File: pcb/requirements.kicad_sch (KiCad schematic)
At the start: 14 parts

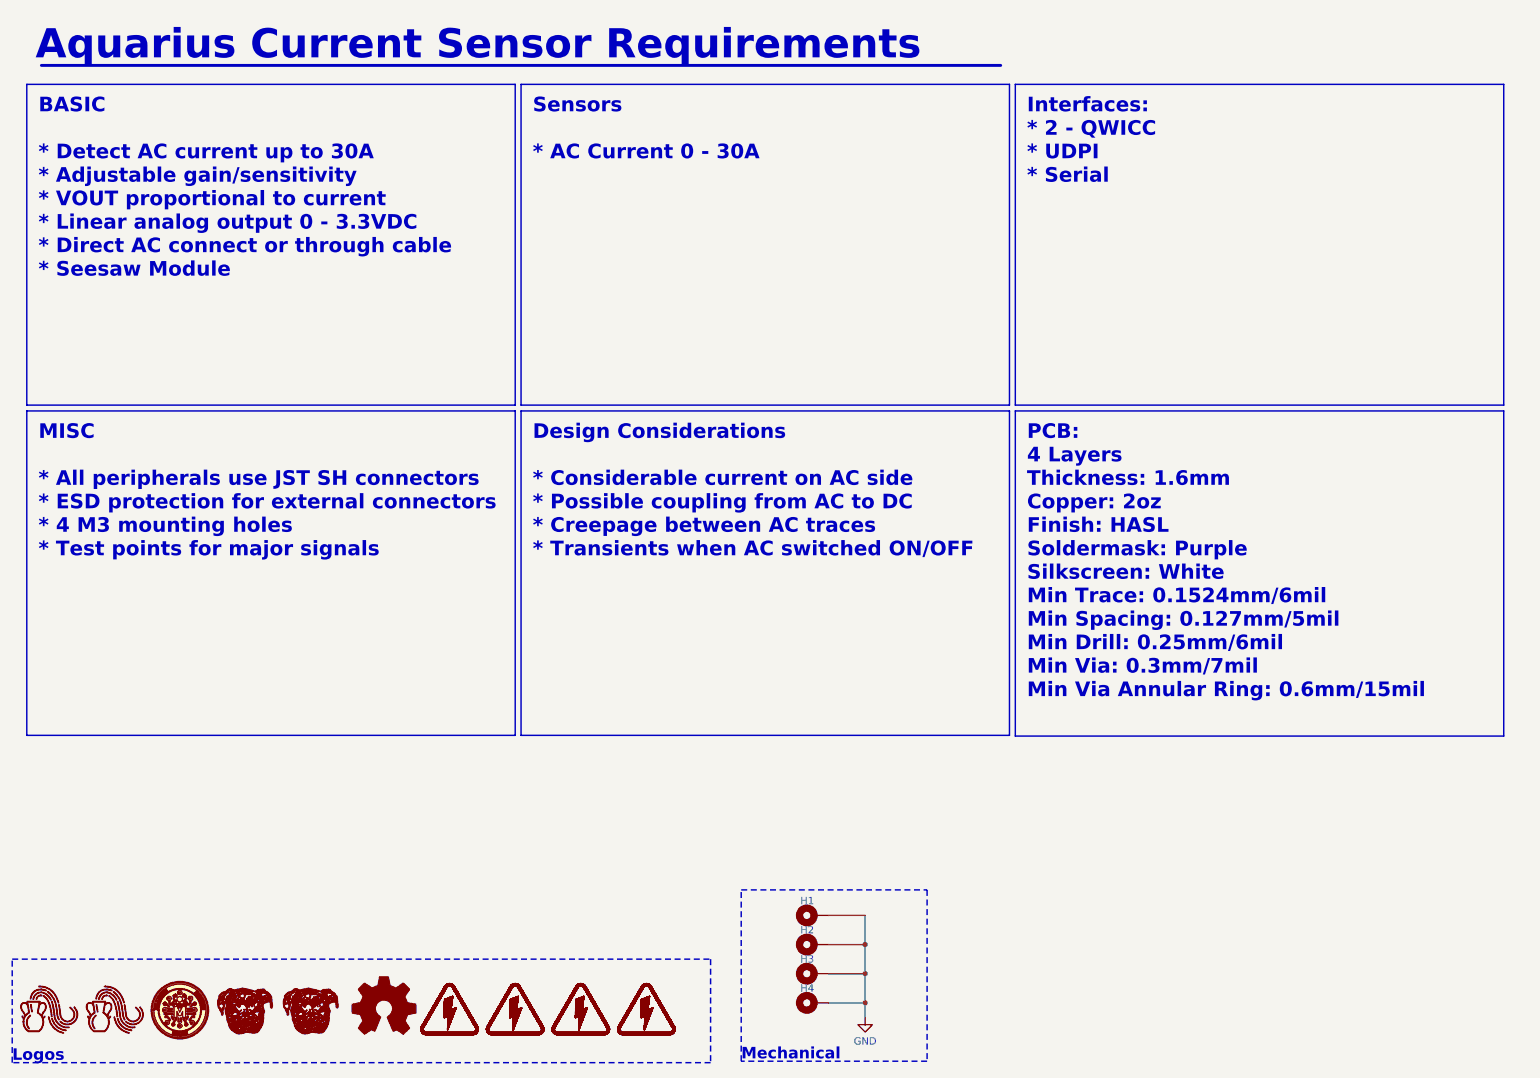
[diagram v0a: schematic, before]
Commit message: refactored to STM32
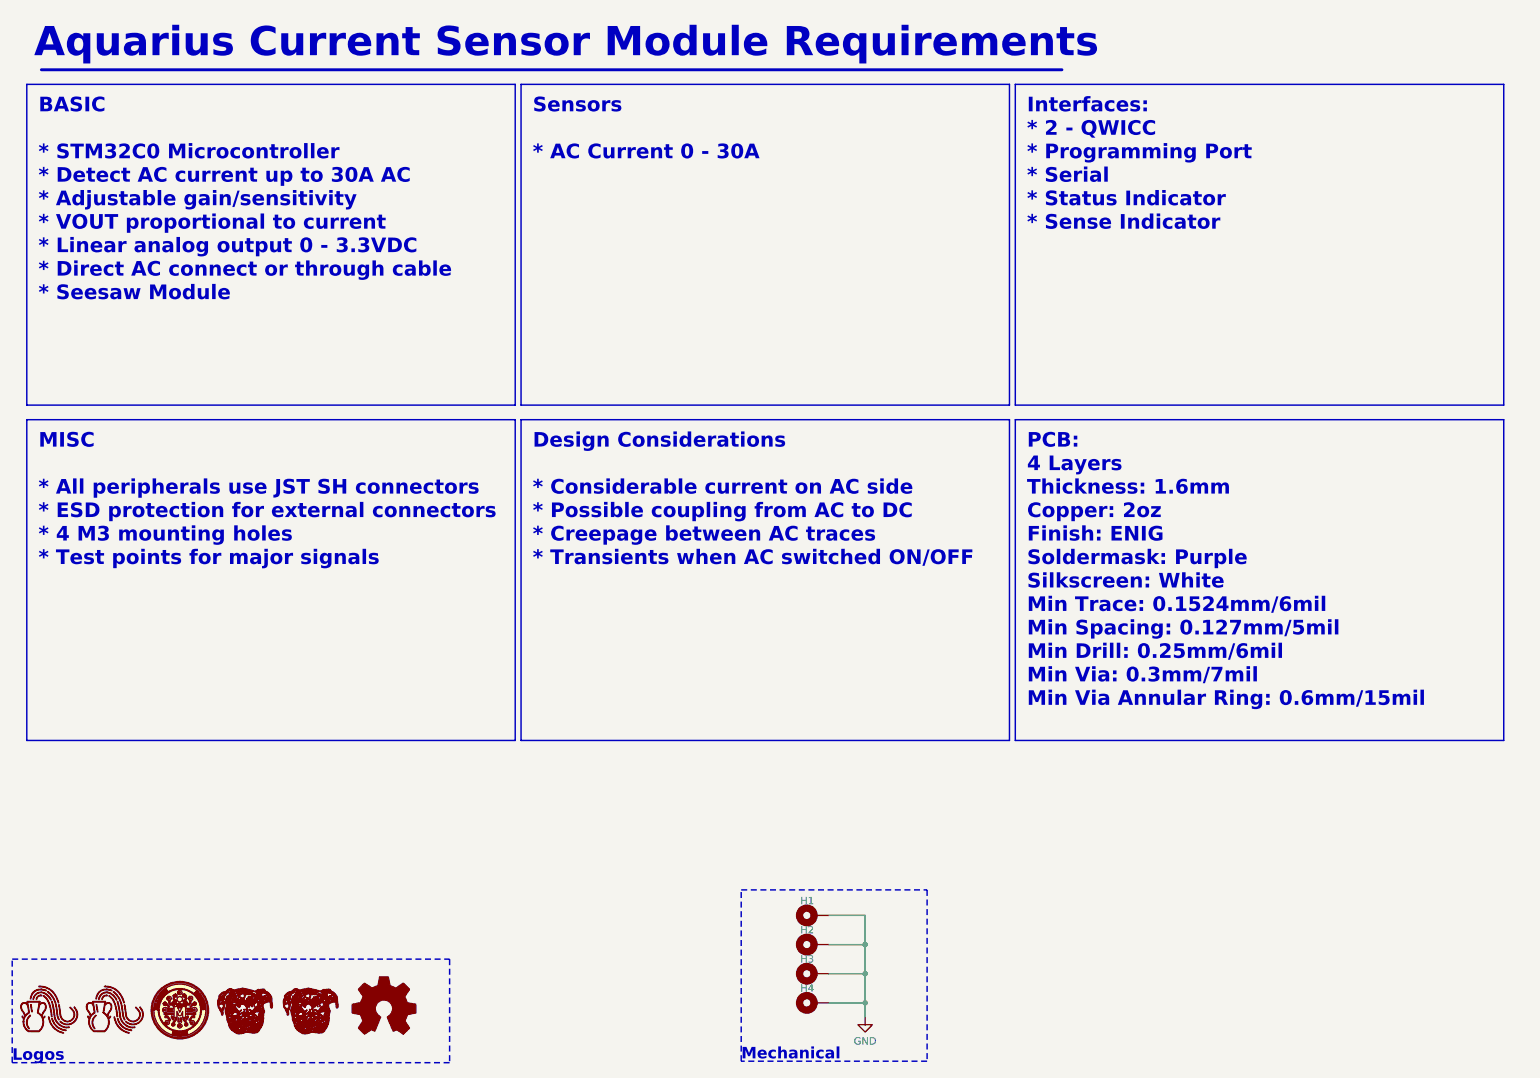
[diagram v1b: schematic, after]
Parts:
- removed SYM1, SYM2, SYM3, SYM4: ~, CRGM Symbols:HIGH-VOLTAGE-5MM, symbol CRGM Symbols:High Voltage
- H1, H2, H3, H4, LOGO1, LOGO3, LOGO4, LOGO5: value ~ -> (none)
- LOGO2: value ~ -> (none); footprint CRGM Logos:Roxy 4mm -> CRGM Logos:Roxy 6.5mm
- LOGO7: value ~ -> (none); footprint CRGM Logos:Aquarius Logo 3.5mm -> CRGM Logos:Aquarius Logo 5mm
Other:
- note added: "Aquarius Current Sensor Module Requirements"
- note removed: "Aquarius Current Sensor Requirements"

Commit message: Added additional silkscreen to AC side
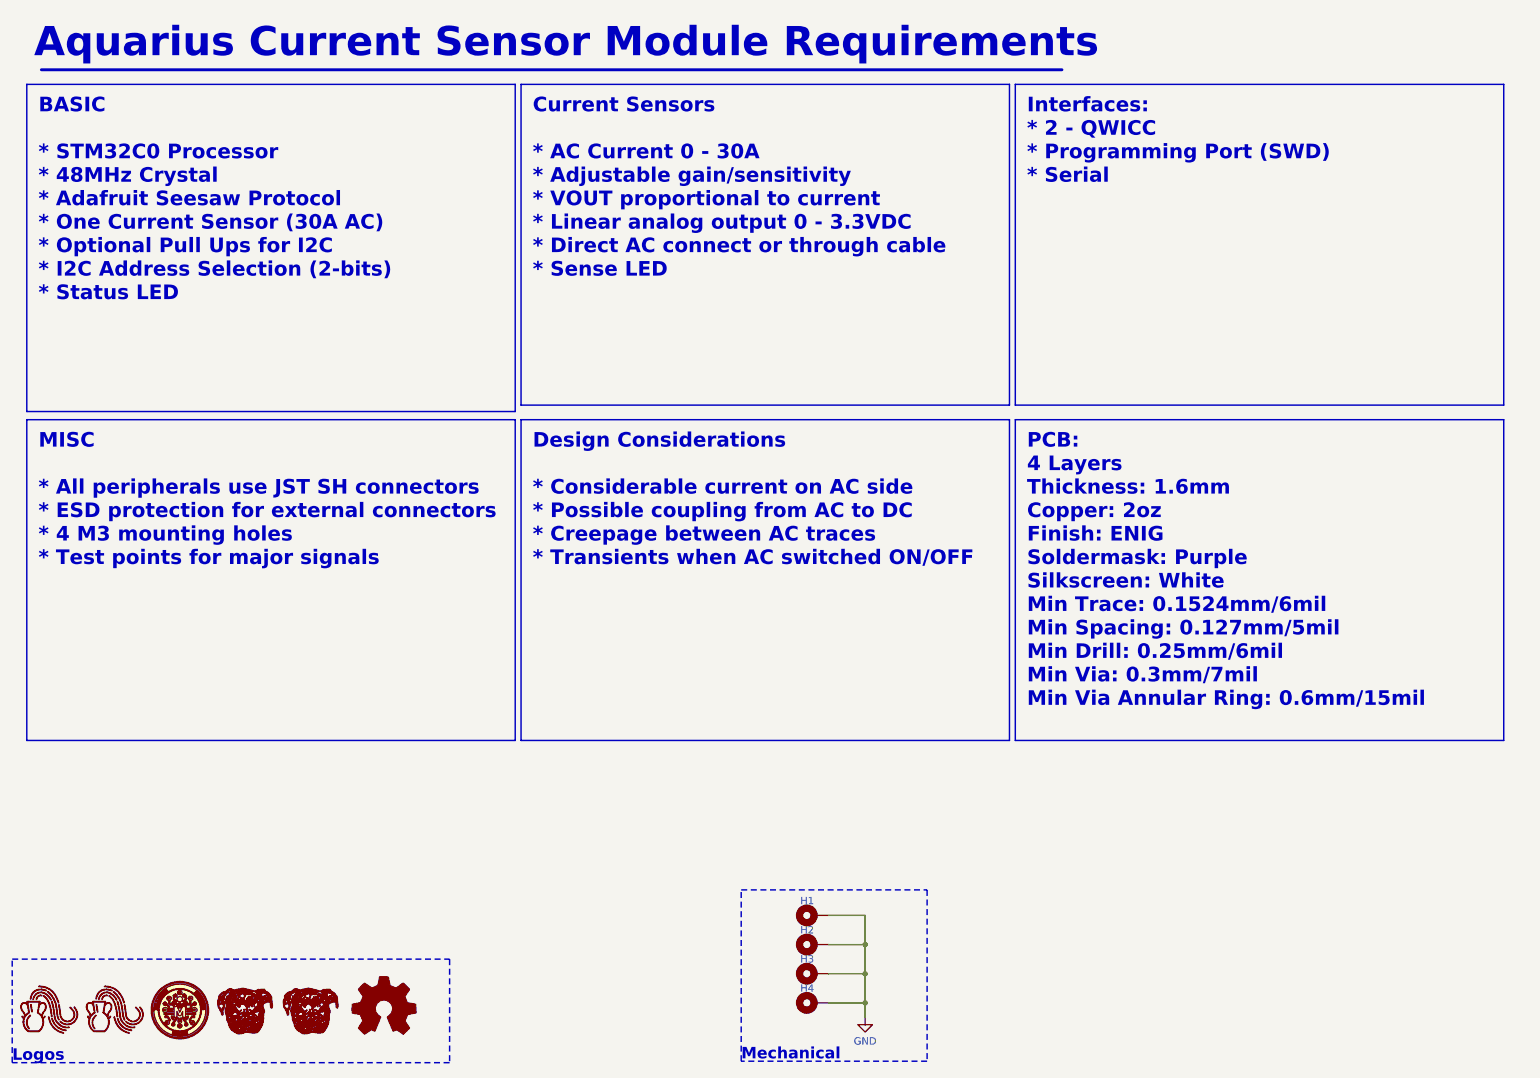
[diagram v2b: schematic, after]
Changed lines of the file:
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@@
 		)
 	)
-	(text_box "Interfaces:\n* 2 - QWICC\n* Programming Port\n* Serial\n* Status Indicator\n* Sense Indicator"
+	(text_box "Interfaces:\n* 2 - QWICC\n* Programming Port (SWD)\n* Serial\n"
 		(exclude_from_sim yes)
 		(at 189.992 25.4 0)
@@
 		)
 	)
-	(text_box "BASIC\n\n* STM32C0 Microcontroller\n* Detect AC current up to 30A AC\n* Adjustable gain/sensitivity\n* VOUT proportional to current\n* Linear analog output 0 - 3.3VDC\n* Direct AC connect or through cable\n* Seesaw Module"
+	(text_box "BASIC\n\n* STM32C0 Processor\n* 48MHz Crystal\n* Adafruit Seesaw Protocol\n* One Current Sensor (30A AC)\n* Optional Pull Ups for I2C\n* I2C Address Selection (2-bits)\n* Status LED"
 		(exclude_from_sim yes)
 		(at 17.78 25.4 0)
-		(size 85.09 55.88)
+		(size 85.09 56.9984)
 		(margins 2.032 2.032 2.032 2.032)
 		(stroke
@@
 		)
 	)
-	(text_box "Sensors\n\n* AC Current 0 - 30A\n"
+	(text_box "Current Sensors\n\n* AC Current 0 - 30A\n* Adjustable gain/sensitivity\n* VOUT proportional to current\n* Linear analog output 0 - 3.3VDC\n* Direct AC connect or through cable\n* Sense LED\n"
 		(exclude_from_sim yes)
 		(at 103.886 25.4 0)

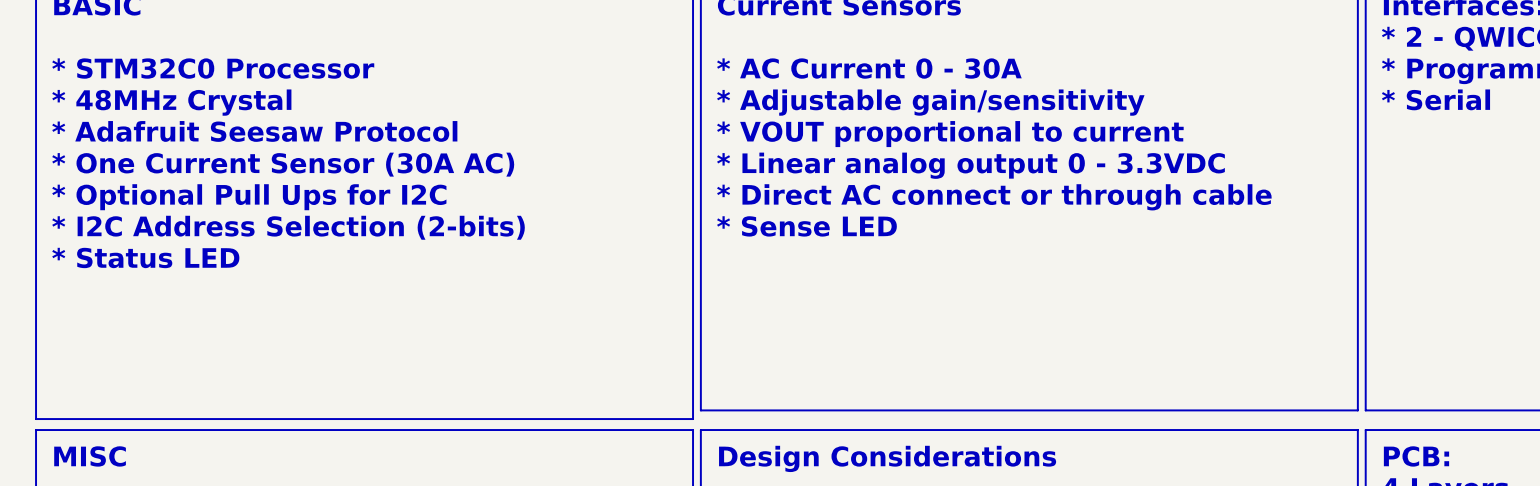
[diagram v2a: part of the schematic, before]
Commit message: Removed AC input via copper
Testing revealed sending AC through copper did not trigger device. Removed ability to send AC through the PCB.
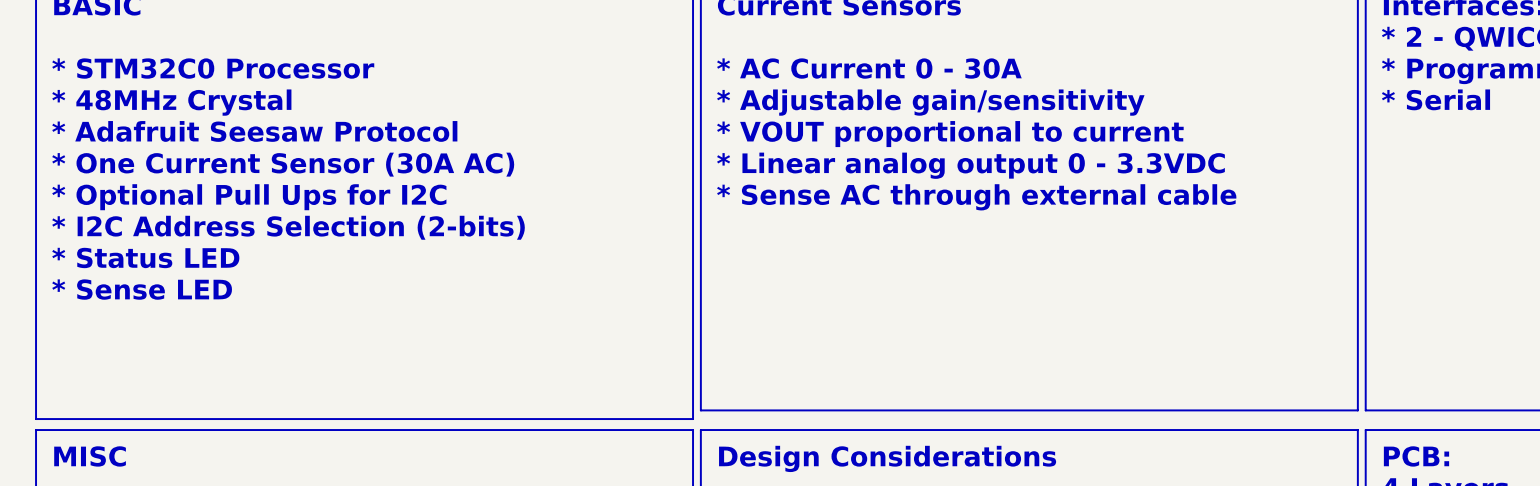
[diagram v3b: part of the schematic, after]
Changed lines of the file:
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@@
 		)
 	)
-	(text_box "BASIC\n\n* STM32C0 Processor\n* 48MHz Crystal\n* Adafruit Seesaw Protocol\n* One Current Sensor (30A AC)\n* Optional Pull Ups for I2C\n* I2C Address Selection (2-bits)\n* Status LED"
+	(text_box "BASIC\n\n* STM32C0 Processor\n* 48MHz Crystal\n* Adafruit Seesaw Protocol\n* One Current Sensor (30A AC)\n* Optional Pull Ups for I2C\n* I2C Address Selection (2-bits)\n* Status LED\n* Sense LED"
 		(exclude_from_sim yes)
 		(at 17.78 25.4 0)
@@
 		)
 	)
-	(text_box "Current Sensors\n\n* AC Current 0 - 30A\n* Adjustable gain/sensitivity\n* VOUT proportional to current\n* Linear analog output 0 - 3.3VDC\n* Direct AC connect or through cable\n* Sense LED\n"
+	(text_box "Current Sensors\n\n* AC Current 0 - 30A\n* Adjustable gain/sensitivity\n* VOUT proportional to current\n* Linear analog output 0 - 3.3VDC\n* Sense AC through external cable\n"
 		(exclude_from_sim yes)
 		(at 103.886 25.4 0)
